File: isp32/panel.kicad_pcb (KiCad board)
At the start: 2 copper layers, 73 x 102 mm, 222 parts, among them J1 BAT1, J10 LoRa_ANT, J12 Micro_SD_Card, J2 Switching, J3 USB_C_Receptacle_USB2.0, J4 ADC, J5 GPS_ANT, J6 F0, J7 F1, J8 BUZZ, J9 ANT, M1 Motor_Servo, M2 Motor_Servo, M3 Motor_Servo, M4 Motor_Servo, Q1 BSS138, Q2 S8050, Q3 IRLML6402, Q4 BSS138, Q5 IRLML6402, Q6 IRLML6402, Q7 IRLML6402, SW1 RST, U1 AZ1117-3.3, U10 BMP280, U11 MPU-9250, U2 MP2315, U3 STM32G030F6, U6 24LC32, U7 NEO-XM, U8 ESP32-S3-WROOM-1U, U9 RFM98W-315S2

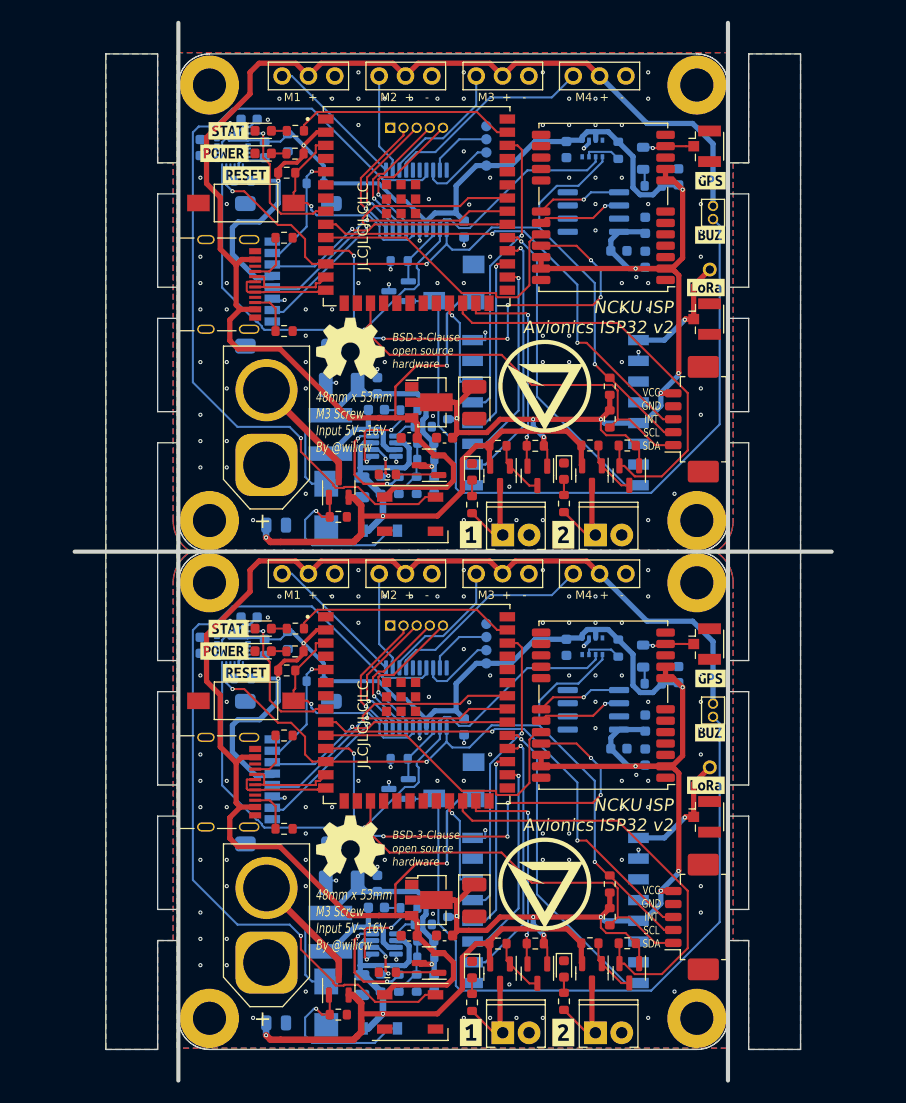
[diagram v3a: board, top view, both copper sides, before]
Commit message: feat: add level converter to imu
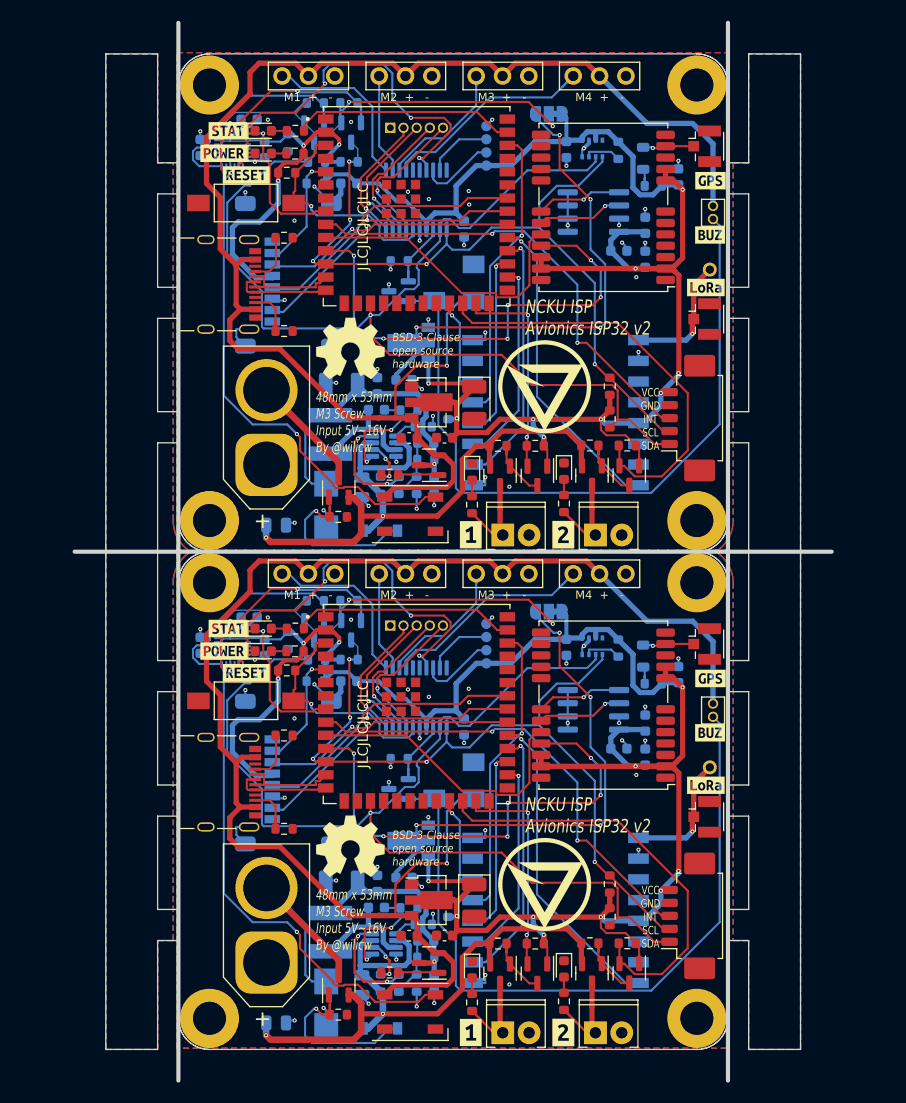
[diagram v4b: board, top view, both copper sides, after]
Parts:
- removed the C1 at (103.2, 61.6)
- removed the C1 at (103.2, 109.6)
- removed the C10 at (104.2, 57.0)
- removed the C10 at (104.2, 105.0)
- removed the C11 at (121.0, 39.0)
- removed the C11 at (121.0, 87.0)
- removed the C12 at (107.0, 53.6)
- removed the C12 at (107.0, 101.6)
- removed the C13 at (123.5, 36.5)
- removed the C13 at (123.5, 84.5)
- removed the C14 at (126.7, 31.9)
- removed the C14 at (126.7, 79.9)
- removed the C15 at (87.9, 113.4)
- removed the C15 at (87.9, 65.4)
- removed the C16 at (115.9, 77.2)
- removed the C16 at (115.9, 29.2)
- removed the C2 at (94.2, 99.9)
- removed the C2 at (94.2, 51.9)
- removed the C22 at (86.8, 29.2)
- removed the C22 at (86.8, 77.2)
- removed the C23 at (80.6, 29.0)
- removed the C23 at (80.6, 77.0)
- removed the C24 at (85.3, 74.3)
- removed the C24 at (85.3, 26.3)
- removed the C3 at (106.1, 84.9)
- removed the C3 at (106.1, 36.9)
- removed the C4 at (97.6, 54.3)
- removed the C4 at (97.6, 102.3)
- removed the C5 at (96.2, 61.8)
- removed the C5 at (96.2, 109.8)
- removed the C6 at (100.8, 57.0)
- removed the C6 at (100.8, 105.0)
- removed the C7 at (102.4, 57.5)
- removed the C7 at (102.4, 105.5)
- removed the C8 at (97.7, 52.0)
- removed the C8 at (97.7, 100.0)
- removed the C9 at (123.5, 39.8)
- removed the C9 at (123.5, 87.8)
- removed the D1 at (98.0, 114.0)
- removed the D1 at (98.0, 66.0)
- removed the D2 at (115.7, 60.2)
- removed the D2 at (115.7, 108.2)
- removed the D3 at (86.7, 75.4)
- removed the D3 at (86.7, 27.4)
- removed the D4 at (106.8, 60.3)
- removed the D4 at (106.8, 108.3)
- removed the D5 at (86.7, 77.6)
- removed the D5 at (86.7, 29.6)
- removed the D6 at (92.8, 111.6)
- removed the D6 at (92.8, 63.6)
- removed the D7 at (100.8, 64.4)
- removed the D7 at (100.8, 112.4)
- removed the G*** at (113.8, 100.0)
- removed the G*** at (113.8, 52.0)
- removed the H1 at (81.5, 23.0)
- removed the H1 at (81.5, 71.0)
- removed the H2 at (81.5, 113.0)
- removed the H2 at (81.5, 65.0)
- removed the H3 at (128.5, 65.0)
- removed the H3 at (128.5, 113.0)
- removed the H4 at (128.5, 23.0)
- removed the H4 at (128.5, 71.0)
- removed the J1 at (87.0, 59.6)
- removed the J1 at (87.0, 107.6)
- removed the J10 at (129.2, 45.6)
- removed the J10 at (129.2, 93.6)
- removed the J12 at (89.7, 41.3)
- removed the J12 at (89.7, 89.3)
- removed the J2 at (128.6, 55.2)
- removed the J2 at (128.6, 103.2)
- removed the J3 at (83.4, 42.2)
- removed the J3 at (83.4, 90.2)
- removed the J4 at (104.0, 75.1)
- removed the J4 at (104.0, 27.1)
- removed the J5 at (129.2, 76.9)
- removed the J5 at (129.2, 28.9)
- removed the J6 at (118.7, 114.4)
- removed the J6 at (118.7, 66.4)
- removed the J7 at (109.8, 66.4)
- removed the J7 at (109.8, 114.4)
- removed the J8 at (130.1, 34.7)
- removed the J8 at (130.1, 82.7)
- removed the J9 at (129.7, 88.8)
- removed the J9 at (129.7, 40.8)
- removed the L2 at (123.3, 78.1)
- removed the L2 at (123.3, 30.1)
- removed the L3 at (93.2, 56.7)
- removed the L3 at (93.2, 104.7)
- removed the LS1 at (105.1, 42.0)
- removed the LS1 at (105.1, 90.0)
- removed the M1 at (88.5, 22.1)
- removed the M1 at (88.5, 70.1)
- removed the M2 at (97.9, 70.1)
- removed the M2 at (97.9, 22.1)
- removed the M3 at (107.2, 70.1)
- removed the M3 at (107.2, 22.1)
- removed the M4 at (116.6, 70.1)
- removed the M4 at (116.6, 22.1)
- removed the Q1 at (122.0, 60.7)
- removed the Q1 at (122.0, 108.7)
- removed the Q2 at (99.7, 42.9)
- removed the Q2 at (99.7, 90.9)
- removed the Q3 at (118.4, 108.7)
- removed the Q3 at (118.4, 60.7)
- removed the Q4 at (113.1, 108.7)
- removed the Q4 at (113.1, 60.7)
- removed the Q5 at (109.5, 108.7)
- removed the Q5 at (109.5, 60.7)
- removed the Q6 at (94.0, 61.8)
- removed the Q6 at (94.0, 109.8)
- removed the Q7 at (102.7, 107.7)
- removed the Q7 at (102.7, 59.7)
- removed the R1 at (88.9, 79.5)
- removed the R1 at (88.9, 31.5)
- removed the R10 at (101.5, 109.6)
- removed the R10 at (101.5, 61.6)
- removed the R11 at (102.4, 59.1)
- removed the R11 at (102.4, 107.1)
- removed the R12 at (124.3, 80.7)
- removed the R12 at (124.3, 32.7)
- removed the R14 at (120.9, 29.3)
- removed the R14 at (120.9, 77.3)
- removed the R15 at (104.5, 102.4)
- removed the R15 at (104.5, 54.4)
- removed the R16 at (121.8, 57.8)
- removed the R16 at (121.8, 105.8)
- removed the R17 at (84.7, 80.2)
- removed the R17 at (84.7, 32.2)
- removed the R18 at (89.7, 77.6)
- removed the R18 at (89.7, 29.6)
- removed the R19 at (89.8, 27.4)
- removed the R19 at (89.8, 75.4)
- removed the R2 at (89.1, 76.6)
- removed the R2 at (89.1, 28.6)
- removed the R20 at (118.2, 105.8)
- removed the R20 at (118.2, 57.8)
- removed the R21 at (102.1, 103.9)
- removed the R21 at (102.1, 55.9)
- removed the R22 at (115.7, 111.4)
- removed the R22 at (115.7, 63.4)
- removed the R23 at (112.9, 57.8)
- removed the R23 at (112.9, 105.8)
- removed the R24 at (109.3, 57.8)
- removed the R24 at (109.3, 105.8)
- removed the R25 at (106.8, 63.5)
- removed the R25 at (106.8, 111.5)
- removed the R26 at (93.9, 112.6)
- removed the R26 at (93.9, 64.6)
- removed the R27 at (98.7, 60.6)
- removed the R27 at (98.7, 108.6)
- removed the R3 at (98.0, 61.6)
- removed the R3 at (98.0, 109.6)
- removed the R30 at (91.7, 80.5)
- removed the R30 at (91.7, 32.5)
- removed the R33 at (99.8, 40.0)
- removed the R33 at (99.8, 88.0)
- removed the R4 at (120.1, 55.2)
- removed the R4 at (120.1, 103.2)
- removed the R5 at (88.7, 85.7)
- removed the R5 at (88.7, 37.7)
- removed the R6 at (120.1, 52.1)
- removed the R6 at (120.1, 100.1)
- removed the R7 at (88.7, 46.7)
- removed the R7 at (88.7, 94.7)
- removed the R8 at (100.7, 102.4)
- removed the R8 at (100.7, 54.4)
- removed the R9 at (99.8, 109.6)
- removed the R9 at (99.8, 61.6)
- removed the SW1 at (85.0, 34.4)
- removed the SW1 at (85.0, 82.4)
- removed the TP1 at (108.2, 30.8)
- removed the TP1 at (108.2, 78.8)
- removed the TP3 at (108.2, 77.5)
- removed the TP3 at (108.2, 29.5)
- removed the TP4 at (108.2, 28.2)
- removed the TP4 at (108.2, 76.2)
- removed the TP5 at (108.2, 75.0)
- removed the TP5 at (108.2, 27.0)
- removed the U1 at (102.6, 101.6)
- removed the U1 at (102.6, 53.6)
- removed the U10 at (118.4, 77.1)
- removed the U10 at (118.4, 29.1)
- removed the U11 at (83.7, 29.3)
- removed the U11 at (83.7, 77.3)
- removed the U2 at (98.3, 57.8)
- removed the U2 at (98.3, 105.8)
- removed the U3 at (101.4, 82.1)
- removed the U3 at (101.4, 34.1)
- removed the U6 at (118.5, 83.2)
- removed the U6 at (118.5, 35.2)
- removed the U7 at (119.5, 82.8)
- removed the U7 at (119.5, 34.8)
- removed the U8 at (101.5, 34.7)
- removed the U8 at (101.5, 82.7)
- removed the U9 at (114.9, 54.6)
- removed the U9 at (114.9, 102.6)
- added C1: 22u, Capacitor_SMD:C_0603_1608Metric, B.Cu at (103.2, 109.6)
- added C1: 22u, Capacitor_SMD:C_0603_1608Metric, B.Cu at (103.2, 61.6)
- added C10: 22u, Capacitor_SMD:C_0603_1608Metric, F.Cu at (104.2, 57.0)
- added C10: 22u, Capacitor_SMD:C_0603_1608Metric, F.Cu at (104.2, 105.0)
- added C11: 100n, Capacitor_SMD:C_0603_1608Metric, B.Cu at (121.0, 39.0)
- added C11: 100n, Capacitor_SMD:C_0603_1608Metric, B.Cu at (121.0, 87.0)
- added C12: 220u, Capacitor_Tantalum_SMD:CP_EIA-3528-12_Kemet-T, F.Cu at (107.0, 101.6)
- added C12: 220u, Capacitor_Tantalum_SMD:CP_EIA-3528-12_Kemet-T, F.Cu at (107.0, 53.6)
- added C13: 100n, Capacitor_SMD:C_0603_1608Metric, B.Cu at (123.5, 84.5)
- added C13: 100n, Capacitor_SMD:C_0603_1608Metric, B.Cu at (123.5, 36.5)
- added C14: 1u, Capacitor_SMD:C_0603_1608Metric, B.Cu at (126.7, 79.9)
- added C14: 1u, Capacitor_SMD:C_0603_1608Metric, B.Cu at (126.7, 31.9)
- added C15: 10u, Capacitor_SMD:C_0805_2012Metric, B.Cu at (87.9, 65.4)
- added C15: 10u, Capacitor_SMD:C_0805_2012Metric, B.Cu at (87.9, 113.4)
- added C16: 100n, Capacitor_SMD:C_0603_1608Metric, B.Cu at (115.9, 29.2)
- added C16: 100n, Capacitor_SMD:C_0603_1608Metric, B.Cu at (115.9, 77.2)
- added C17: 22u, Capacitor_SMD:C_0603_1608Metric, B.Cu at (94.9, 32.5)
- added C17: 22u, Capacitor_SMD:C_0603_1608Metric, B.Cu at (94.9, 80.5)
- added C18: 22u, Capacitor_SMD:C_0603_1608Metric, B.Cu at (100.3, 51.4)
- added C18: 22u, Capacitor_SMD:C_0603_1608Metric, B.Cu at (100.3, 99.4)
- added C2: 220u, Capacitor_Tantalum_SMD:CP_EIA-3528-12_Kemet-T, B.Cu at (94.2, 99.9)
- added C2: 220u, Capacitor_Tantalum_SMD:CP_EIA-3528-12_Kemet-T, B.Cu at (94.2, 51.9)
- added C22: 10n, Capacitor_SMD:C_0603_1608Metric, B.Cu at (86.8, 29.2)
- added C22: 10n, Capacitor_SMD:C_0603_1608Metric, B.Cu at (86.8, 77.2)
- added C23: 100n, Capacitor_SMD:C_0603_1608Metric, B.Cu at (80.6, 77.0)
- added C23: 100n, Capacitor_SMD:C_0603_1608Metric, B.Cu at (80.6, 29.0)
- added C24: 100n, Capacitor_SMD:C_0603_1608Metric, B.Cu at (85.3, 26.3)
- added C24: 100n, Capacitor_SMD:C_0603_1608Metric, B.Cu at (85.3, 74.3)
- added C3: 100n, Capacitor_SMD:C_0603_1608Metric, B.Cu at (106.1, 84.9)
- added C3: 100n, Capacitor_SMD:C_0603_1608Metric, B.Cu at (106.1, 36.9)
- added C4: 100n, Capacitor_SMD:C_0603_1608Metric, B.Cu at (97.6, 54.3)
- added C4: 100n, Capacitor_SMD:C_0603_1608Metric, B.Cu at (97.6, 102.3)
- added C5: 100n, Capacitor_SMD:C_0805_2012Metric, B.Cu at (96.2, 61.8)
- added C5: 100n, Capacitor_SMD:C_0805_2012Metric, B.Cu at (96.2, 109.8)
- added C6: 22u, Capacitor_SMD:C_0603_1608Metric, F.Cu at (100.8, 105.0)
- added C6: 22u, Capacitor_SMD:C_0603_1608Metric, F.Cu at (100.8, 57.0)
- added C7: NC, Capacitor_SMD:C_0603_1608Metric, B.Cu at (102.4, 105.5)
- added C7: NC, Capacitor_SMD:C_0603_1608Metric, B.Cu at (102.4, 57.5)
- added C8: 22u, Capacitor_SMD:C_0603_1608Metric, B.Cu at (97.7, 52.0)
- added C8: 22u, Capacitor_SMD:C_0603_1608Metric, B.Cu at (97.7, 100.0)
- added C9: 100n, Capacitor_SMD:C_0603_1608Metric, B.Cu at (123.5, 87.8)
- added C9: 100n, Capacitor_SMD:C_0603_1608Metric, B.Cu at (123.5, 39.8)
- added D1: Zener, Diode_SMD:D_SOD-123, B.Cu at (98.0, 66.0)
- added D1: Zener, Diode_SMD:D_SOD-123, B.Cu at (98.0, 114.0)
- added D2: F0_LED, LED_SMD:LED_0603_1608Metric, F.Cu at (115.7, 60.2)
- added D2: F0_LED, LED_SMD:LED_0603_1608Metric, F.Cu at (115.7, 108.2)
- added D3: ESP_LED, LED_SMD:LED_0603_1608Metric, F.Cu at (86.7, 27.4)
- added D3: ESP_LED, LED_SMD:LED_0603_1608Metric, F.Cu at (86.7, 75.4)
- added D4: F1_LED, LED_SMD:LED_0603_1608Metric, F.Cu at (106.8, 60.3)
- added D4: F1_LED, LED_SMD:LED_0603_1608Metric, F.Cu at (106.8, 108.3)
- added D5: POWER, LED_SMD:LED_0603_1608Metric, F.Cu at (86.7, 29.6)
- added D5: POWER, LED_SMD:LED_0603_1608Metric, F.Cu at (86.7, 77.6)
- added D6: TVS, Diode_SMD:D_SMB, B.Cu at (92.8, 63.6)
- added D6: TVS, Diode_SMD:D_SMB, B.Cu at (92.8, 111.6)
- added D7: WS2812B, LED_SMD:LED_WS2812B_PLCC4_5.0x5.0mm_P3.2mm, F.Cu at (100.8, 112.4)
- added D7: WS2812B, LED_SMD:LED_WS2812B_PLCC4_5.0x5.0mm_P3.2mm, F.Cu at (100.8, 64.4)
- added G***: LOGO, isp_logo:isp_logo, F.Cu at (113.8, 52.1)
- added G***: LOGO, isp_logo:isp_logo, F.Cu at (113.8, 100.1)
- added H1: MountingHole_Pad, MountingHole:MountingHole_3.2mm_M3_ISO7380_Pad, F.Cu at (81.5, 23.0)
- added H1: MountingHole_Pad, MountingHole:MountingHole_3.2mm_M3_ISO7380_Pad, F.Cu at (81.5, 71.0)
- added H2: MountingHole_Pad, MountingHole:MountingHole_3.2mm_M3_ISO7380_Pad, F.Cu at (81.5, 65.0)
- added H2: MountingHole_Pad, MountingHole:MountingHole_3.2mm_M3_ISO7380_Pad, F.Cu at (81.5, 113.0)
- added H3: MountingHole_Pad, MountingHole:MountingHole_3.2mm_M3_ISO7380_Pad, F.Cu at (128.5, 113.0)
- added H3: MountingHole_Pad, MountingHole:MountingHole_3.2mm_M3_ISO7380_Pad, F.Cu at (128.5, 65.0)
- added H4: MountingHole_Pad, MountingHole:MountingHole_3.2mm_M3_ISO7380_Pad, F.Cu at (128.5, 71.0)
- added H4: MountingHole_Pad, MountingHole:MountingHole_3.2mm_M3_ISO7380_Pad, F.Cu at (128.5, 23.0)
- added J1: BAT1, Connector_AMASS:AMASS_XT60-M_1x02_P7.20mm_Vertical, F.Cu at (87.0, 59.6)
- added J1: BAT1, Connector_AMASS:AMASS_XT60-M_1x02_P7.20mm_Vertical, F.Cu at (87.0, 107.6)
- added J10: LoRa_ANT, Connector_Coaxial:U.FL_Hirose_U.FL-R-SMT-1_Vertical, F.Cu at (129.2, 45.6)
- added J10: LoRa_ANT, Connector_Coaxial:U.FL_Hirose_U.FL-R-SMT-1_Vertical, F.Cu at (129.2, 93.6)
- added J12: Micro_SD_Card, Connector_Card:microSD_HC_Molex_47219-2001, B.Cu at (89.7, 89.3)
- added J12: Micro_SD_Card, Connector_Card:microSD_HC_Molex_47219-2001, B.Cu at (89.7, 41.3)
- added J2: Switching, Connector_Molex:Molex_PicoBlade_53261-0571_1x05-1MP_P1.25mm_Horizontal, F.Cu at (128.3, 55.1)
- added J2: Switching, Connector_Molex:Molex_PicoBlade_53261-0571_1x05-1MP_P1.25mm_Horizontal, F.Cu at (128.3, 103.1)
- added J3: USB_C_Receptacle_USB2.0, Connector_USB:USB_C_Receptacle_Palconn_UTC16-G, F.Cu at (83.4, 42.2)
- added J3: USB_C_Receptacle_USB2.0, Connector_USB:USB_C_Receptacle_Palconn_UTC16-G, F.Cu at (83.4, 90.2)
- added J4: ADC, Connector_PinHeader_1.27mm:PinHeader_1x05_P1.27mm_Vertical, B.Cu at (104.0, 75.1)
- added J4: ADC, Connector_PinHeader_1.27mm:PinHeader_1x05_P1.27mm_Vertical, B.Cu at (104.0, 27.1)
- added J5: GPS_ANT, Connector_Coaxial:U.FL_Hirose_U.FL-R-SMT-1_Vertical, F.Cu at (129.2, 28.9)
- added J5: GPS_ANT, Connector_Coaxial:U.FL_Hirose_U.FL-R-SMT-1_Vertical, F.Cu at (129.2, 76.9)
- added J6: F0, TerminalBlock_Phoenix:TerminalBlock_Phoenix_MPT-0,5-2-2.54_1x02_P2.54mm_Horizontal, F.Cu at (118.7, 114.4)
- added J6: F0, TerminalBlock_Phoenix:TerminalBlock_Phoenix_MPT-0,5-2-2.54_1x02_P2.54mm_Horizontal, F.Cu at (118.7, 66.4)
- added J7: F1, TerminalBlock_Phoenix:TerminalBlock_Phoenix_MPT-0,5-2-2.54_1x02_P2.54mm_Horizontal, F.Cu at (109.8, 114.4)
- added J7: F1, TerminalBlock_Phoenix:TerminalBlock_Phoenix_MPT-0,5-2-2.54_1x02_P2.54mm_Horizontal, F.Cu at (109.8, 66.4)
- added J8: BUZZ, Connector_PinHeader_1.27mm:PinHeader_1x02_P1.27mm_Vertical, F.Cu at (130.1, 34.7)
- added J8: BUZZ, Connector_PinHeader_1.27mm:PinHeader_1x02_P1.27mm_Vertical, F.Cu at (130.1, 82.7)
- added J9: ANT, Connector_PinHeader_2.00mm:PinHeader_1x01_P2.00mm_Vertical, F.Cu at (129.7, 88.8)
- added J9: ANT, Connector_PinHeader_2.00mm:PinHeader_1x01_P2.00mm_Vertical, F.Cu at (129.7, 40.8)
- added JP1: MPU VIO, Jumper:SolderJumper-3_P1.3mm_Bridged12_RoundedPad1.0x1.5mm_NumberLabels, B.Cu at (114.2, 25.8)
- added JP1: MPU VIO, Jumper:SolderJumper-3_P1.3mm_Bridged12_RoundedPad1.0x1.5mm_NumberLabels, B.Cu at (114.2, 73.8)
- added L2: NC, Inductor_SMD:L_0805_2012Metric, B.Cu at (123.3, 78.1)
- added L2: NC, Inductor_SMD:L_0805_2012Metric, B.Cu at (123.3, 30.1)
- added L3: 5.5, Inductor_SMD:L_Sunlord_SWPA5020S, B.Cu at (93.2, 104.7)
- added L3: 5.5, Inductor_SMD:L_Sunlord_SWPA5020S, B.Cu at (93.2, 56.7)
- added LS1: 5020, Buzzer:XDCR_KSSG33J12-3, B.Cu at (105.1, 90.0)
- added LS1: 5020, Buzzer:XDCR_KSSG33J12-3, B.Cu at (105.1, 42.0)
- added M1: Motor_Servo, Connector_PinHeader_2.54mm:PinHeader_1x03_P2.54mm_Vertical, F.Cu at (88.5, 70.1)
- added M1: Motor_Servo, Connector_PinHeader_2.54mm:PinHeader_1x03_P2.54mm_Vertical, F.Cu at (88.5, 22.1)
- added M2: Motor_Servo, Connector_PinHeader_2.54mm:PinHeader_1x03_P2.54mm_Vertical, F.Cu at (97.9, 22.1)
- added M2: Motor_Servo, Connector_PinHeader_2.54mm:PinHeader_1x03_P2.54mm_Vertical, F.Cu at (97.9, 70.1)
- added M3: Motor_Servo, Connector_PinHeader_2.54mm:PinHeader_1x03_P2.54mm_Vertical, F.Cu at (107.2, 22.1)
- added M3: Motor_Servo, Connector_PinHeader_2.54mm:PinHeader_1x03_P2.54mm_Vertical, F.Cu at (107.2, 70.1)
- added M4: Motor_Servo, Connector_PinHeader_2.54mm:PinHeader_1x03_P2.54mm_Vertical, F.Cu at (116.6, 70.1)
- added M4: Motor_Servo, Connector_PinHeader_2.54mm:PinHeader_1x03_P2.54mm_Vertical, F.Cu at (116.6, 22.1)
- added Q1: BSS138, Package_TO_SOT_SMD:SOT-23, F.Cu at (122.0, 108.7)
- added Q1: BSS138, Package_TO_SOT_SMD:SOT-23, F.Cu at (122.0, 60.7)
- added Q2: S8050, Package_TO_SOT_SMD:SOT-23, B.Cu at (99.7, 90.9)
- added Q2: S8050, Package_TO_SOT_SMD:SOT-23, B.Cu at (99.7, 42.9)
- added Q3: IRLML6402, Package_TO_SOT_SMD:SOT-23, F.Cu at (118.4, 60.7)
- added Q3: IRLML6402, Package_TO_SOT_SMD:SOT-23, F.Cu at (118.4, 108.7)
- added Q4: BSS138, Package_TO_SOT_SMD:SOT-23, F.Cu at (113.1, 108.7)
- added Q4: BSS138, Package_TO_SOT_SMD:SOT-23, F.Cu at (113.1, 60.7)
- added Q5: IRLML6402, Package_TO_SOT_SMD:SOT-23, F.Cu at (109.5, 60.7)
- added Q5: IRLML6402, Package_TO_SOT_SMD:SOT-23, F.Cu at (109.5, 108.7)
- added Q6: IRLML6402, Package_TO_SOT_SMD:SOT-23, F.Cu at (94.0, 61.8)
- added Q6: IRLML6402, Package_TO_SOT_SMD:SOT-23, F.Cu at (94.0, 109.8)
- added Q7: IRLML6402, Package_TO_SOT_SMD:SOT-23, F.Cu at (102.7, 59.7)
- added Q7: IRLML6402, Package_TO_SOT_SMD:SOT-23, F.Cu at (102.7, 107.7)
- added Q8: BSS138, Package_TO_SOT_SMD:SOT-23, B.Cu at (91.6, 75.6)
- added Q8: BSS138, Package_TO_SOT_SMD:SOT-23, B.Cu at (91.6, 27.6)
- added Q9: BSS138, Package_TO_SOT_SMD:SOT-23, B.Cu at (95.2, 27.6)
- added Q9: BSS138, Package_TO_SOT_SMD:SOT-23, B.Cu at (95.2, 75.6)
- added R1: 10k, Resistor_SMD:R_0603_1608Metric, F.Cu at (88.9, 31.5)
- added R1: 10k, Resistor_SMD:R_0603_1608Metric, F.Cu at (88.9, 79.5)
- added R10: 7k5, Resistor_SMD:R_0603_1608Metric, B.Cu at (101.5, 61.6)
- added R10: 7k5, Resistor_SMD:R_0603_1608Metric, B.Cu at (101.5, 109.6)
- added R11: 40.2k, Resistor_SMD:R_0603_1608Metric, B.Cu at (102.4, 59.1)
- added R11: 40.2k, Resistor_SMD:R_0603_1608Metric, B.Cu at (102.4, 107.1)
- added R12: NC, Resistor_SMD:R_0603_1608Metric, B.Cu at (124.3, 80.7)
- added R12: NC, Resistor_SMD:R_0603_1608Metric, B.Cu at (124.3, 32.7)
- added R13: 10k, Resistor_SMD:R_0603_1608Metric, B.Cu at (91.7, 24.7)
- added R13: 10k, Resistor_SMD:R_0603_1608Metric, B.Cu at (91.7, 72.7)
- added R14: 10k, Resistor_SMD:R_0603_1608Metric, B.Cu at (120.9, 29.3)
- added R14: 10k, Resistor_SMD:R_0603_1608Metric, B.Cu at (120.9, 77.3)
- added R15: 10k, Resistor_SMD:R_0603_1608Metric, B.Cu at (104.5, 54.4)
- added R15: 10k, Resistor_SMD:R_0603_1608Metric, B.Cu at (104.5, 102.4)
- added R16: 100K, Resistor_SMD:R_0603_1608Metric, F.Cu at (121.8, 57.8)
- added R16: 100K, Resistor_SMD:R_0603_1608Metric, F.Cu at (121.8, 105.8)
- added R17: 10k, Resistor_SMD:R_0603_1608Metric, B.Cu at (94.9, 72.7)
- added R17: 10k, Resistor_SMD:R_0603_1608Metric, B.Cu at (94.9, 24.7)
- added R18: 1k, Resistor_SMD:R_0603_1608Metric, F.Cu at (89.7, 77.6)
- added R18: 1k, Resistor_SMD:R_0603_1608Metric, F.Cu at (89.7, 29.6)
- added R19: 1k, Resistor_SMD:R_0603_1608Metric, F.Cu at (89.8, 75.4)
- added R19: 1k, Resistor_SMD:R_0603_1608Metric, F.Cu at (89.8, 27.4)
- added R2: 10k, Resistor_SMD:R_0603_1608Metric, B.Cu at (89.1, 28.6)
- added R2: 10k, Resistor_SMD:R_0603_1608Metric, B.Cu at (89.1, 76.6)
- added R20: 100K, Resistor_SMD:R_0603_1608Metric, F.Cu at (118.2, 57.8)
- added R20: 100K, Resistor_SMD:R_0603_1608Metric, F.Cu at (118.2, 105.8)
- added R21: 75k, Resistor_SMD:R_0603_1608Metric, B.Cu at (102.1, 55.9)
- added R21: 75k, Resistor_SMD:R_0603_1608Metric, B.Cu at (102.1, 103.9)
- added R22: 10k, Resistor_SMD:R_0603_1608Metric, F.Cu at (115.7, 63.4)
- added R22: 10k, Resistor_SMD:R_0603_1608Metric, F.Cu at (115.7, 111.4)
- added R23: 100K, Resistor_SMD:R_0603_1608Metric, F.Cu at (112.9, 57.8)
- added R23: 100K, Resistor_SMD:R_0603_1608Metric, F.Cu at (112.9, 105.8)
- added R24: 100K, Resistor_SMD:R_0603_1608Metric, F.Cu at (109.3, 57.8)
- added R24: 100K, Resistor_SMD:R_0603_1608Metric, F.Cu at (109.3, 105.8)
- added R25: 10k, Resistor_SMD:R_0603_1608Metric, F.Cu at (106.8, 63.5)
- added R25: 10k, Resistor_SMD:R_0603_1608Metric, F.Cu at (106.8, 111.5)
- added R26: 100k, Resistor_SMD:R_0603_1608Metric, F.Cu at (93.9, 64.6)
- added R26: 100k, Resistor_SMD:R_0603_1608Metric, F.Cu at (93.9, 112.6)
- added R27: 100k, Resistor_SMD:R_0603_1608Metric, F.Cu at (98.9, 108.6)
- added R27: 100k, Resistor_SMD:R_0603_1608Metric, F.Cu at (98.9, 60.6)
- added R28: 10k, Resistor_SMD:R_0603_1608Metric, B.Cu at (91.8, 30.4)
- added R28: 10k, Resistor_SMD:R_0603_1608Metric, B.Cu at (91.8, 78.4)
- added R29: 10k, Resistor_SMD:R_0603_1608Metric, B.Cu at (95.0, 78.4)
- added R29: 10k, Resistor_SMD:R_0603_1608Metric, B.Cu at (95.0, 30.4)
- added R3: 100k, Resistor_SMD:R_0603_1608Metric, B.Cu at (98.0, 61.6)
- added R3: 100k, Resistor_SMD:R_0603_1608Metric, B.Cu at (98.0, 109.6)
- added R30: 10k, Resistor_SMD:R_0603_1608Metric, B.Cu at (91.7, 80.5)
- added R30: 10k, Resistor_SMD:R_0603_1608Metric, B.Cu at (91.7, 32.5)
- added R33: 10k, Resistor_SMD:R_0603_1608Metric, B.Cu at (99.8, 40.0)
- added R33: 10k, Resistor_SMD:R_0603_1608Metric, B.Cu at (99.8, 88.0)
- added R4: 4k7, Resistor_SMD:R_0603_1608Metric, F.Cu at (120.1, 55.2)
- added R4: 4k7, Resistor_SMD:R_0603_1608Metric, F.Cu at (120.1, 103.2)
- added R5: 5k1, Resistor_SMD:R_0603_1608Metric, F.Cu at (88.7, 37.7)
- added R5: 5k1, Resistor_SMD:R_0603_1608Metric, F.Cu at (88.7, 85.7)
- added R6: 4k7, Resistor_SMD:R_0603_1608Metric, F.Cu at (120.1, 52.1)
- added R6: 4k7, Resistor_SMD:R_0603_1608Metric, F.Cu at (120.1, 100.1)
- added R7: 5k1, Resistor_SMD:R_0603_1608Metric, F.Cu at (88.7, 94.7)
- added R7: 5k1, Resistor_SMD:R_0603_1608Metric, F.Cu at (88.7, 46.7)
- added R8: 20, Resistor_SMD:R_0603_1608Metric, B.Cu at (100.7, 54.4)
- added R8: 20, Resistor_SMD:R_0603_1608Metric, B.Cu at (100.7, 102.4)
- added R9: 20k, Resistor_SMD:R_0603_1608Metric, B.Cu at (99.8, 109.6)
- added R9: 20k, Resistor_SMD:R_0603_1608Metric, B.Cu at (99.8, 61.6)
- added REF**: WEEE-Logo_4.2x6mm_SilkScreen, Symbol:WEEE-Logo_4.2x6mm_SilkScreen, B.Cu at (112.1, 90.2)
- added REF**: ESD-Logo_6.6x6mm_SilkScreen, Symbol:ESD-Logo_6.6x6mm_SilkScreen, B.Cu at (118.1, 42.3)
- added REF**: ESD-Logo_6.6x6mm_SilkScreen, Symbol:ESD-Logo_6.6x6mm_SilkScreen, B.Cu at (118.1, 90.3)
- added REF**: WEEE-Logo_4.2x6mm_SilkScreen, Symbol:WEEE-Logo_4.2x6mm_SilkScreen, B.Cu at (112.1, 42.2)
- added SW1: RST, Button_Switch_SMD:SW_SPST_FSMSM, F.Cu at (85.0, 82.4)
- added SW1: RST, Button_Switch_SMD:SW_SPST_FSMSM, F.Cu at (85.0, 34.4)
- added TP1: 3V3, TestPoint:TestPoint_Pad_D1.0mm, B.Cu at (108.2, 30.8)
- added TP1: 3V3, TestPoint:TestPoint_Pad_D1.0mm, B.Cu at (108.2, 78.8)
- added TP3: SWDIO, TestPoint:TestPoint_Pad_D1.0mm, B.Cu at (108.2, 29.5)
- added TP3: SWDIO, TestPoint:TestPoint_Pad_D1.0mm, B.Cu at (108.2, 77.5)
- added TP4: SWCLK, TestPoint:TestPoint_Pad_D1.0mm, B.Cu at (108.2, 28.2)
- added TP4: SWCLK, TestPoint:TestPoint_Pad_D1.0mm, B.Cu at (108.2, 76.2)
- added TP5: GND, TestPoint:TestPoint_Pad_D1.0mm, B.Cu at (108.2, 75.0)
- added TP5: GND, TestPoint:TestPoint_Pad_D1.0mm, B.Cu at (108.2, 27.0)
- added U1: AZ1117-3.3, Package_TO_SOT_SMD:SOT-89-3, F.Cu at (102.6, 101.6)
- added U1: AZ1117-3.3, Package_TO_SOT_SMD:SOT-89-3, F.Cu at (102.6, 53.6)
- added U10: BMP280, Package_LGA:Bosch_LGA-8_2x2.5mm_P0.65mm_ClockwisePinNumbering, B.Cu at (118.4, 29.1)
- added U10: BMP280, Package_LGA:Bosch_LGA-8_2x2.5mm_P0.65mm_ClockwisePinNumbering, B.Cu at (118.4, 77.1)
- added U11: MPU-9250, Sensor_Motion:InvenSense_QFN-24_3x3mm_P0.4mm, B.Cu at (83.7, 77.3)
- added U11: MPU-9250, Sensor_Motion:InvenSense_QFN-24_3x3mm_P0.4mm, B.Cu at (83.7, 29.3)
- added U2: MP2315, Package_TO_SOT_SMD:TSOT-23-8, B.Cu at (98.3, 57.8)
- added U2: MP2315, Package_TO_SOT_SMD:TSOT-23-8, B.Cu at (98.3, 105.8)
- added U3: STM32G030F6, Package_SO:TSSOP-20_4.4x6.5mm_P0.65mm, B.Cu at (101.4, 34.1)
- added U3: STM32G030F6, Package_SO:TSSOP-20_4.4x6.5mm_P0.65mm, B.Cu at (101.4, 82.1)
- added U4: AZ1117-1.8, Package_TO_SOT_SMD:SOT-89-3, B.Cu at (101.0, 47.9)
- added U4: AZ1117-1.8, Package_TO_SOT_SMD:SOT-89-3, B.Cu at (101.0, 95.9)
- added U6: 24LC32, Package_SO:SOIC-8_3.9x4.9mm_P1.27mm, B.Cu at (118.5, 35.2)
- added U6: 24LC32, Package_SO:SOIC-8_3.9x4.9mm_P1.27mm, B.Cu at (118.5, 83.2)
- added U7: NEO-XM, RF_GPS:ublox_NEO, F.Cu at (119.5, 34.8)
- added U7: NEO-XM, RF_GPS:ublox_NEO, F.Cu at (119.5, 82.8)
- added U8: ESP32-S3-WROOM-1U, ESP32-S3-WROOM-1U:XCVR_ESP32-S3-WROOM-1U, F.Cu at (101.5, 34.7)
- added U8: ESP32-S3-WROOM-1U, ESP32-S3-WROOM-1U:XCVR_ESP32-S3-WROOM-1U, F.Cu at (101.5, 82.7)
- added U9: RFM98W-315S2, RF_Module:HOPERF_RFM9XW_SMD, B.Cu at (114.9, 102.6)
- added U9: RFM98W-315S2, RF_Module:HOPERF_RFM9XW_SMD, B.Cu at (114.9, 54.6)
- added kibuzzard-642D96EE: G***, kibuzzard-642D96EE, B.Cu at (120.3, 74.6)
- added kibuzzard-642D96EE: G***, kibuzzard-642D96EE, B.Cu at (120.3, 26.6)
- added kibuzzard-642D96F8: G***, kibuzzard-642D96F8, B.Cu at (119.7, 73.1)
- added kibuzzard-642D96F8: G***, kibuzzard-642D96F8, B.Cu at (119.7, 25.1)
- added kibuzzard-642D97EE: G***, kibuzzard-642D97EE, B.Cu at (127.3, 54.1)
- added kibuzzard-642D97EE: G***, kibuzzard-642D97EE, B.Cu at (127.3, 102.1)
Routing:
- net Board_1-+1V8: track 0.00 -> 48.7 mm, vias 0 -> 4
- net Board_0-+1V8: track 0.00 -> 48.7 mm, vias 0 -> 4
- net Board_1-MPU_VIO_SEL: track 0.00 -> 41.5 mm, vias 0 -> 2
- net Board_0-MPU_VIO_SEL: track 0.00 -> 41.5 mm, vias 0 -> 2
- net Board_1-GND: track 16.3 -> 52.5 mm, vias 95 -> 44
- net Board_0-GND: track 16.3 -> 52.5 mm, vias 95 -> 44
- net Board_0-Net-(Q8-Pad2): track 0.00 -> 21.6 mm
- net Board_1-Net-(Q8-Pad2): track 0.00 -> 21.6 mm
- net Board_1-Net-(Q9-Pad2): track 0.00 -> 21.6 mm, vias 0 -> 2
- net Board_0-Net-(Q9-Pad2): track 0.00 -> 21.6 mm, vias 0 -> 2
- net Board_1-+3V3: track 192.0 -> 206.7 mm, vias 10 -> 12
- net Board_0-+3V3: track 192.0 -> 206.7 mm, vias 10 -> 12
- net Board_1-SDA: track 99.7 -> 107.5 mm
- net Board_0-SDA: track 99.7 -> 107.5 mm
- net Board_1-RGB: track 80.6 -> 86.0 mm, vias 1 -> 5
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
